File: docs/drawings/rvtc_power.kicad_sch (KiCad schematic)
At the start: 0 parts

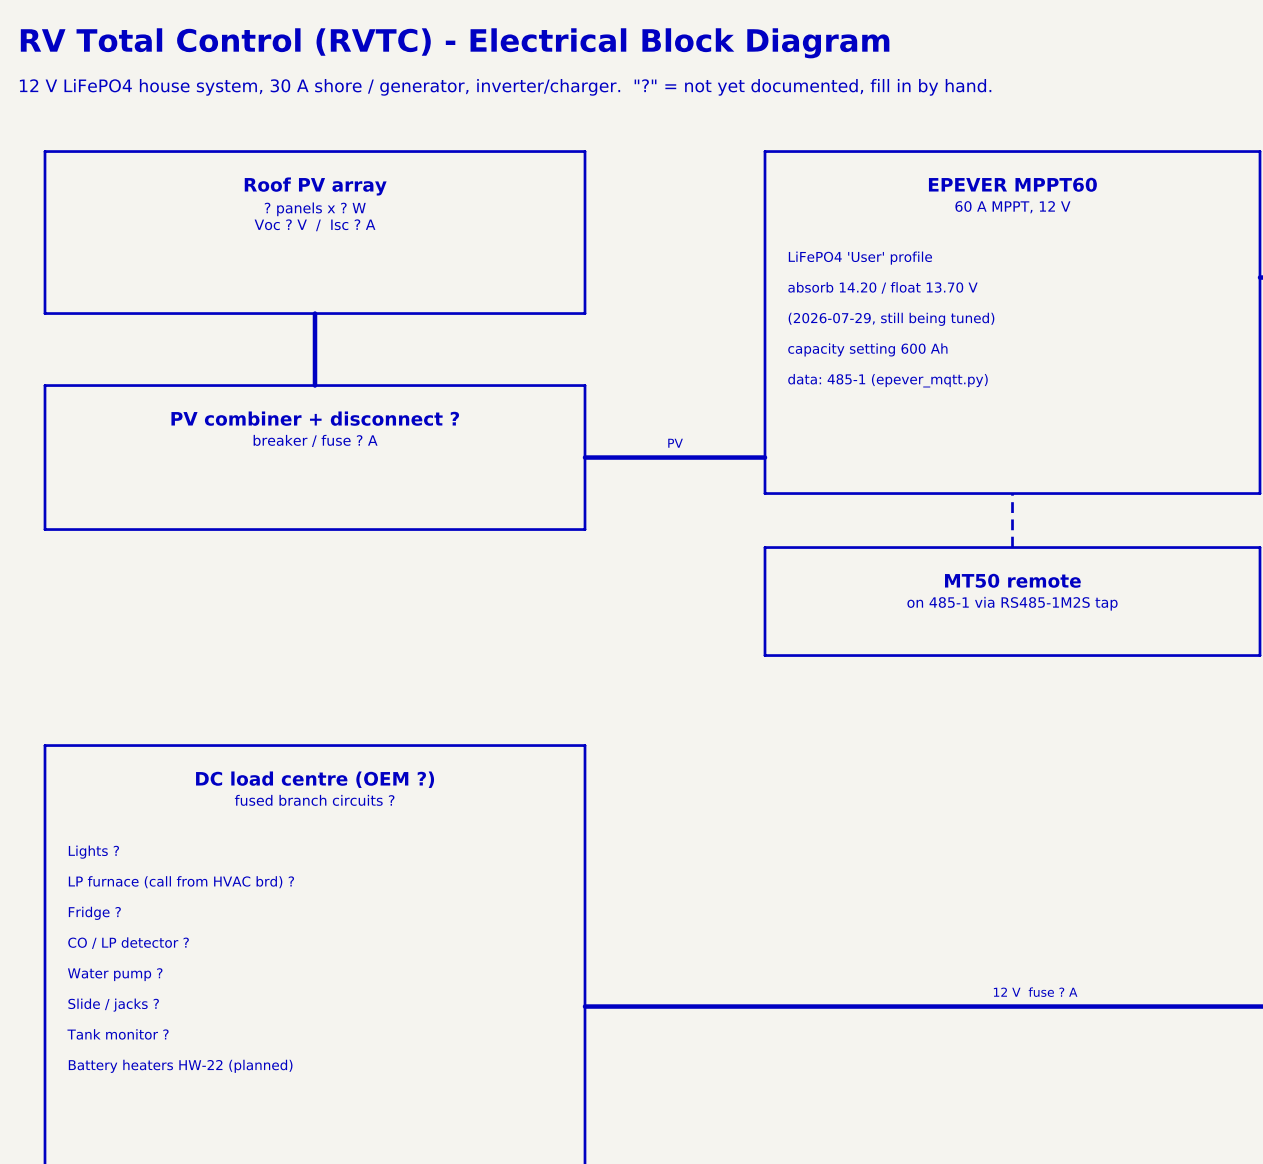
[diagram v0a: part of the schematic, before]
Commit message: Drawings: observer is a LilyGo T-Beam; fill in PV array from datasheet
Page 1: MeshCore Observer box now names VE7CBH-RVTC (LilyGo T-Beam,
DUQ, also reports to the public observer map) instead of "ESP32-S3".

Page 2 (includes the owner's hand edits so far, e.g. DC load centre
fuse 70 A and 3 string lines): PV array is 9 x Renogy RNG-100D-SS,
3S3P = 900 W; array Voc 72.9 V / Isc 15.6 A, Vmp 61.2 V / Imp 14.7 A
(from the panel datasheet). Combiner notes the 15 A panel max series
fuse rating.

Co-Authored-By: Claude Opus 5.5 <noreply@anthropic.com>
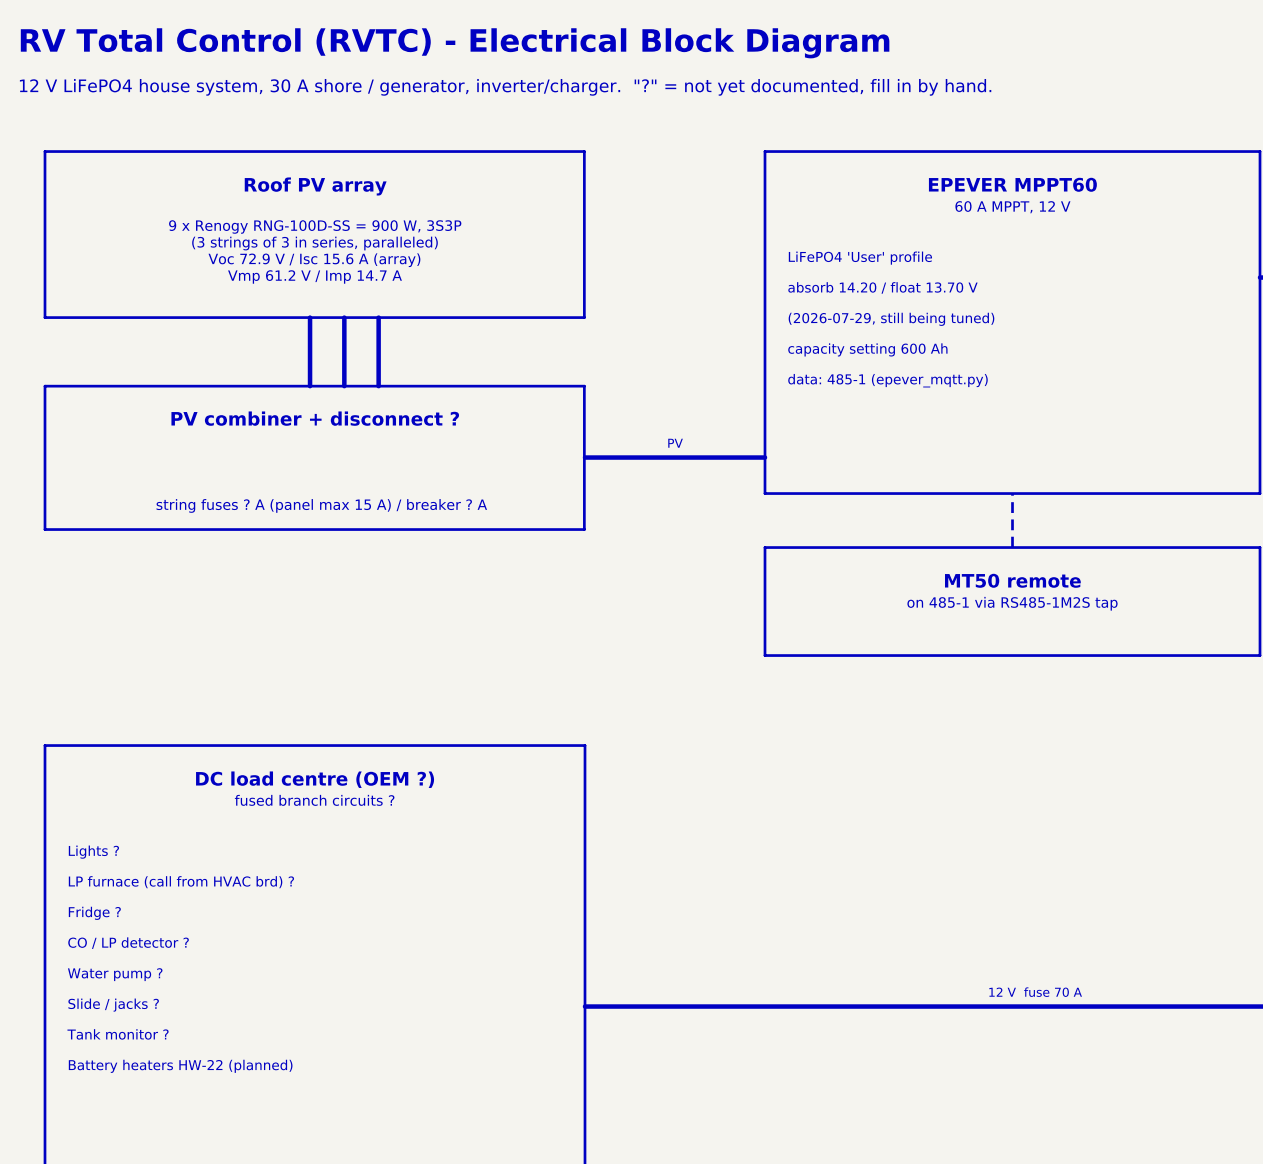
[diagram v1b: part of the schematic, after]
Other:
- note added: "12 V fuse 70 A"
- note added: "9 x Renogy RNG-100D-SS = 900 W, 3S3P (3 strings of 3 in series, paralleled) Voc 72.9 V / Isc 15.6 A (array) Vmp 61.2 V / Imp 14.7 A"
- note added: "string fuses ? A (panel max 15 A) / breaker ? A"
- note removed: "12 V fuse ? A"
- note removed: "? panels x ? W Voc ? V / Isc ? A"
- note removed: "breaker / fuse ? A"

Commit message: Drawings: 11x17, single Waveshare 8-port unit, two DC distributions
- Both sheets now USLedger (11x17); layouts compressed vertically to fit.
- Page 1: the eight 485-x gateways are one Waveshare 8-port RS-485/ETH
  unit (one IP per port), drawn as a single box like the HF5142B.
- Page 2: filled from the parts list (items carried over from the Cougar
  build): 350 A ANL main fuse + Ampper switch, ECO-WORTHY combiner (12 A
  per string), BlueFire fuse box, 30 A shore/gen cords + DIN breakers,
  WFCO OEM load centre, EVO-RC+ remote, Sony/Sceptre monitors. Flags the
  80 V-rated Americal DIN breaker vs ~86 V cold array Voc.
- Two DC distribution points: forward electrical bay bus bars and the
  WFCO OEM load centre, fed through a 250 A main DC fuse.
- Page 1 generator emits 11x17 directly.

Co-Authored-By: Claude Opus 5.5 <noreply@anthropic.com>
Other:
- note added: "2 x 30 A DIN brkr/disconnect + meter, DIN box auto transfer switch, or EVO AC-in priority ?"
- note added: "AC load centre (WFCO, OEM)"
- note added: "BlueFire 12-way blade fuse box, feed ? A - all 12 V"
- note added: "Bsomain ANL-350A + Ampper battery switch (S1)"
- note added: "ECO-WORTHY 4-string, 12 A brkr/string (3 used) Americal 50 A DC DIN brkr ? - rated 80 V!"
- note added: "Forward electrical bay - 12 V DC distribution - +/- bus bars ?"
- note added: "Generator inlet 30 A"
- note added: "Main fuse 350 A ANL"
- note added: "PV combiner + disconnect"
- note added: "Sony 32in HDMI TV/monitor Sceptre 16in (12 V PSU on AC) 1 via HDMI-over-Cat5e ? J45 speakers"
- note added: "Trailer DC distribution (WFCO, OEM)"
- note added: "Waveshare 8-port RS-485 gateway"
- note added: "inverter / charger, 12 V, EVO-RC+ remote"
- note added: "main DC fuse 250 A"
- note removed: "+ battery disconnect ?"
- note removed: "12 V DC distribution - +/- bus bars ?"
- note removed: "12 V fuse 70 A"
- note removed: "2 x J45 monitors (1 via HDMI-over-Cat5e) J45 speakers"
- note removed: "AC load centre (OEM ?)"
- note removed: "DC load centre (OEM ?)"
- note removed: "Generator inlet ? A"
- note removed: "Main fuse ? A"
- note removed: "PV combiner + disconnect ?"
- note removed: "Waveshare RS-485 gateways x8"
- note removed: "auto transfer switch, or EVO AC-in priority ?"
- note removed: "inverter / charger, 12 V"
- note removed: "own fused feed ? A - all RVTC kit is 12 V"
- note removed: "string fuses ? A (panel max 15 A) / breaker ? A"

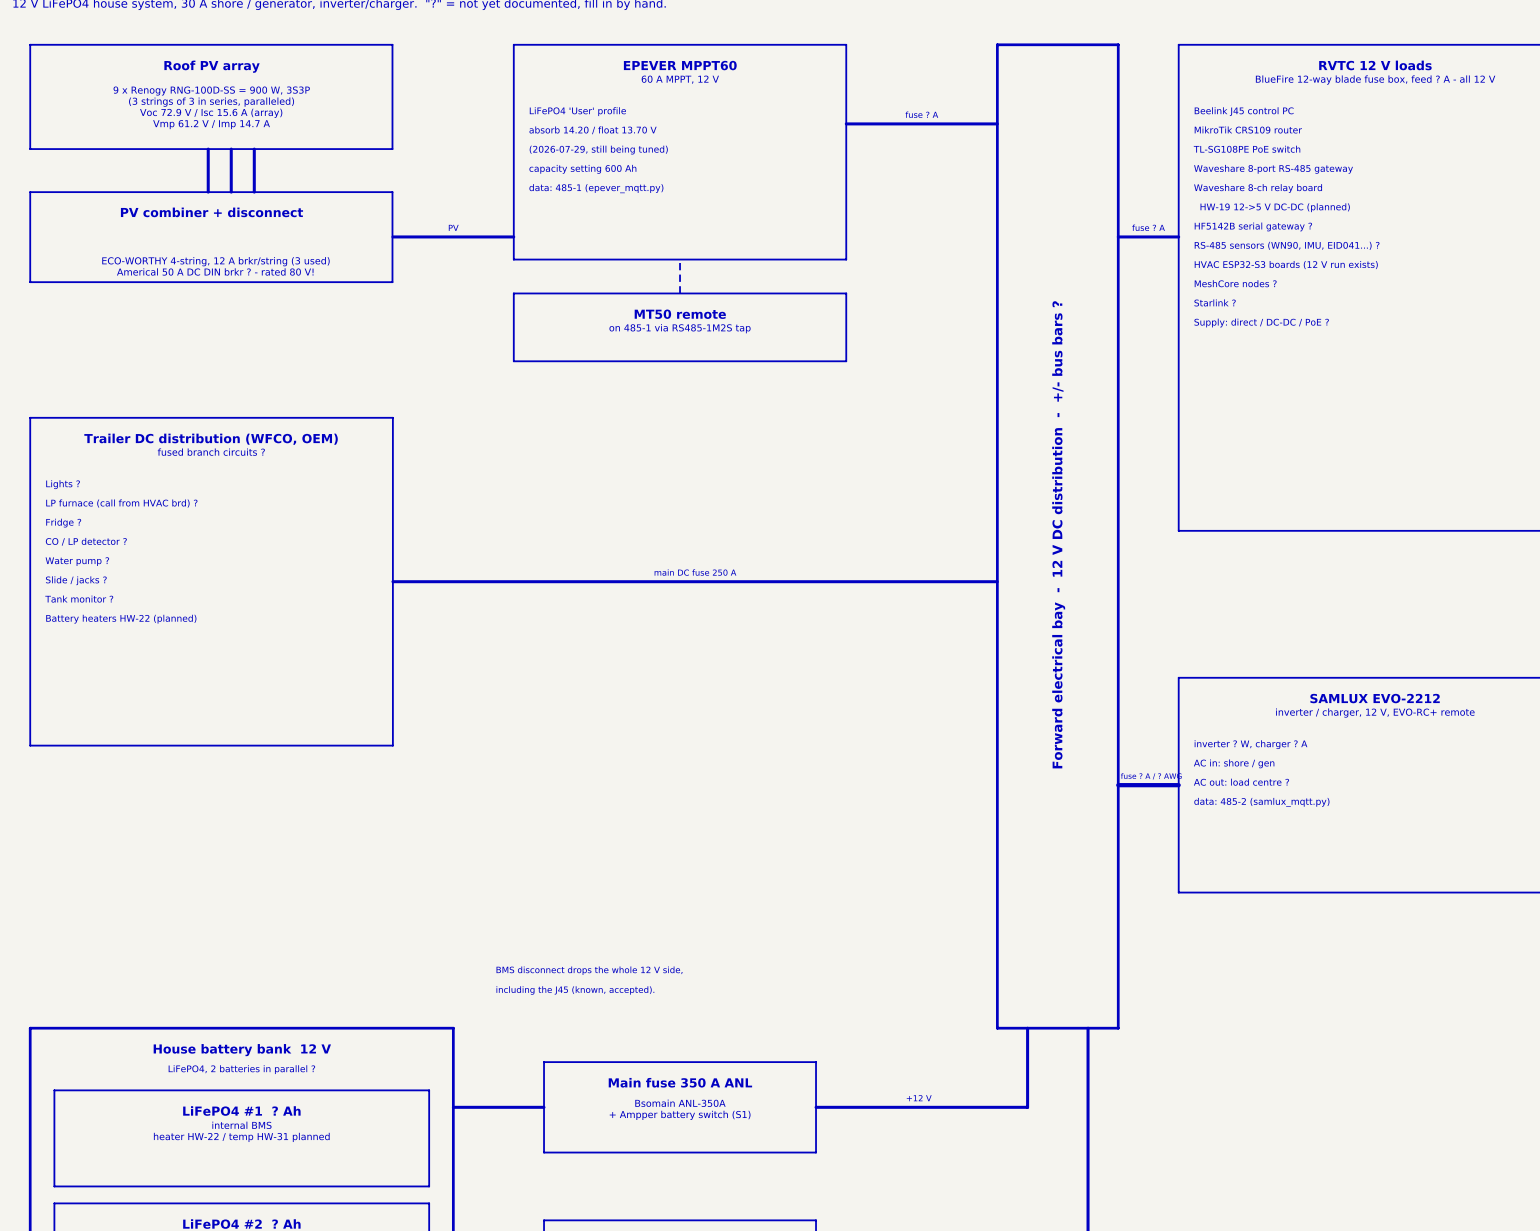
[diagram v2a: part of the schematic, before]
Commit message: Electrical sheet: correct breaker/fuse placement per owner
- PV combiner breakers rated 250 VDC (drops the 80 V warning).
- MPPT60 output: 50 A DC breaker (the Americal DIN unit).
- Ampper S1 + 350 A Class T feeds the EVO-2212 (battery isolation);
  Ampper S2 + 250 A ANL feeds the WFCO trailer DC distribution.
  No other ANL fuses in this build (old 70 A / 100 A were Cougar-only).
- Main battery fuse at the B+ terminal drawn as TBD (type and size).
- RVTC 12 V: 5 V 50 W PSU off the forward fuse block feeds a 5 V
  blade fuse block.

Co-Authored-By: Claude Opus 5.5 <noreply@anthropic.com>
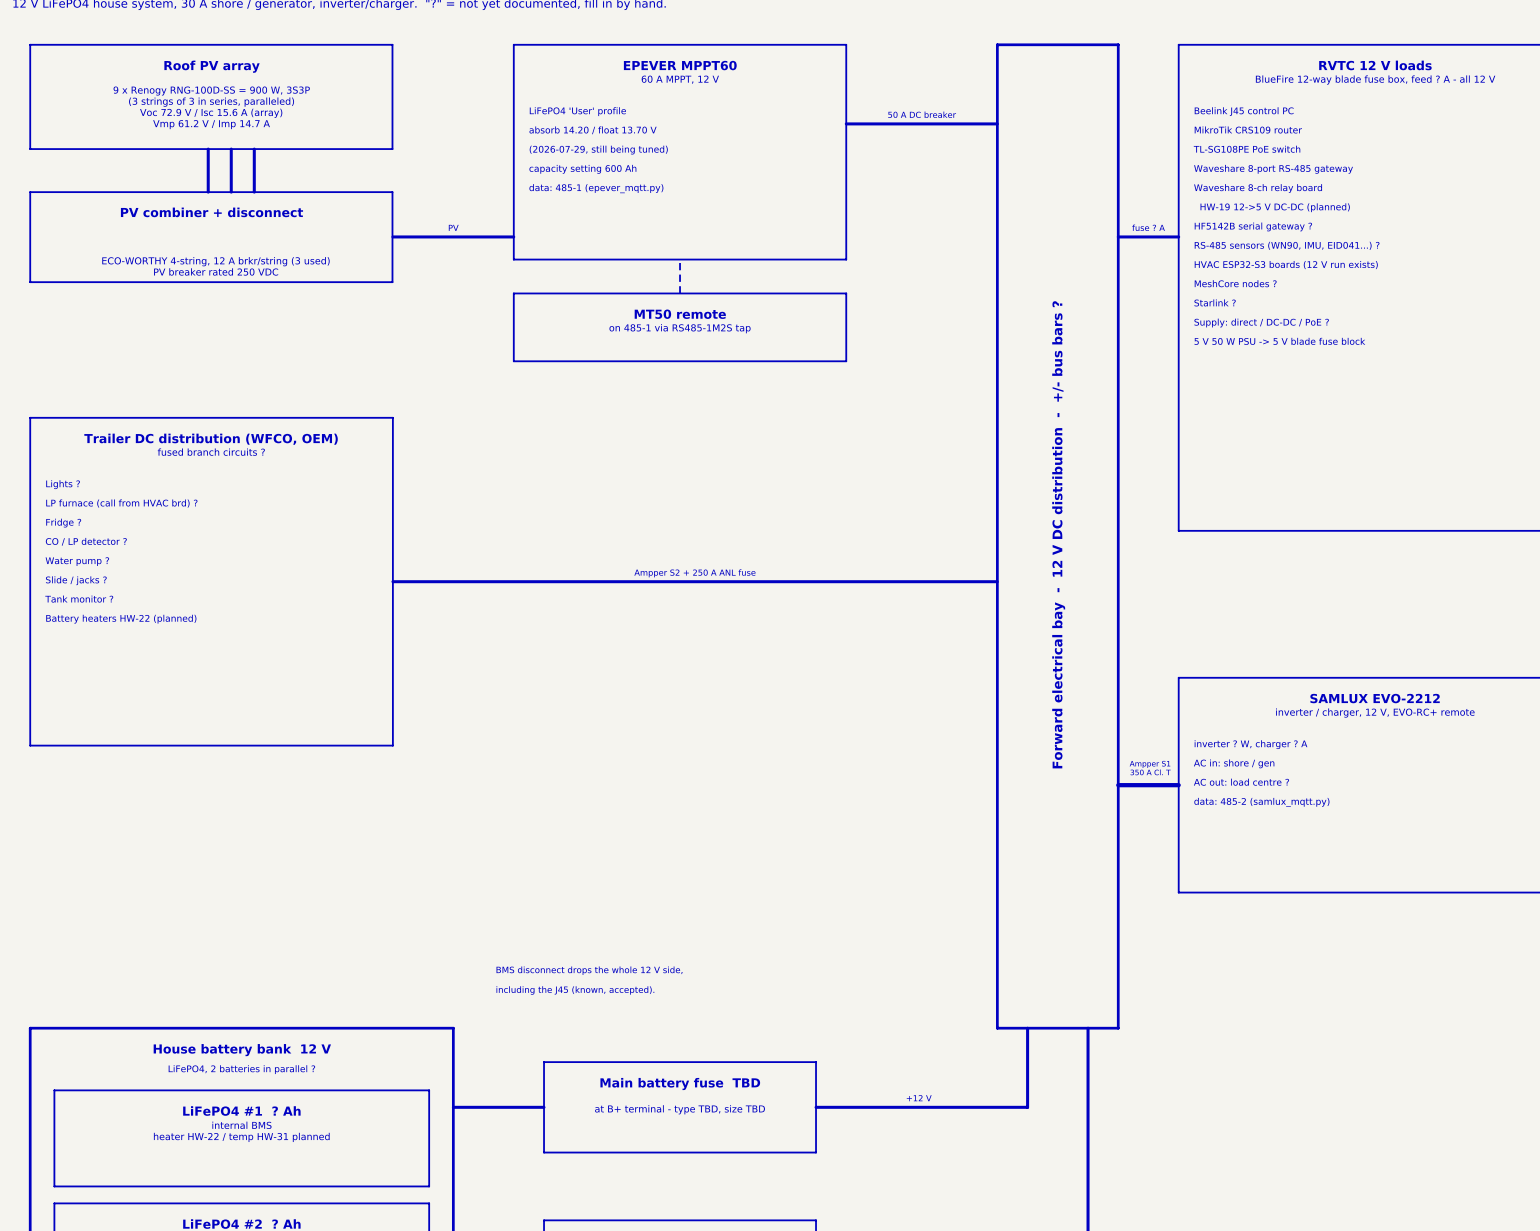
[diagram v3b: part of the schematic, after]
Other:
- note added: "5 V 50 W PSU -> 5 V blade fuse block"
- note added: "50 A DC breaker"
- note added: "Ampper S1 350 A Cl. T"
- note added: "Ampper S2 + 250 A ANL fuse"
- note added: "ECO-WORTHY 4-string, 12 A brkr/string (3 used) PV breaker rated 250 VDC"
- note added: "Main battery fuse TBD"
- note added: "at B+ terminal - type TBD, size TBD"
- note removed: "Bsomain ANL-350A + Ampper battery switch (S1)"
- note removed: "ECO-WORTHY 4-string, 12 A brkr/string (3 used) Americal 50 A DC DIN brkr ? - rated 80 V!"
- note removed: "Main fuse 350 A ANL"
- note removed: "fuse ? A / ? AWG"
- note removed: "main DC fuse 250 A"
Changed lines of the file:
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@@
+		)
+	)
+	(text "5 V 50 W PSU -> 5 V blade fuse block"
+		(exclude_from_sim no)
+		(at 207.5 74.33 0)
+		(effects
+			(font
+				(size 1.1 1.1)
+			)
+			(justify left)
 		)
 	)
@@
 		)
 	)
-	(text "fuse ? A / ? AWG"
-		(exclude_from_sim no)
-		(at 200.5 146.23 0)
+	(text "Ampper S1\n350 A Cl. T"
+		(exclude_from_sim no)
+		(at 200.3 144.9 0)
 		(effects
 			(font
@@
 		)
 	)
-	(text "ECO-WORTHY 4-string, 12 A brkr/string (3 used)\nAmerical 50 A DC DIN brkr ? - rated 80 V!"
+	(text "ECO-WORTHY 4-string, 12 A brkr/string (3 used)\nPV breaker rated 250 VDC"
 		(exclude_from_sim no)
 		(at 45.72 61.922 0)
@@
 		)
 	)
-	(text "Bsomain ANL-350A\n+ Ampper battery switch (S1)"
+	(text "at B+ terminal - type TBD, size TBD"
 		(exclude_from_sim no)
 		(at 122.5 201.301 0)
@@
 		)
 	)
-	(text "Main fuse 350 A ANL"
+	(text "Main battery fuse  TBD"
 		(exclude_from_sim no)
 		(at 122.5 197 0)
@@
 		)
 	)
-	(text "fuse ? A"
+	(text "50 A DC breaker"
 		(exclude_from_sim no)
 		(at 162.5 36.835 0)
@@
 		)
 	)
-	(text "main DC fuse 250 A"
+	(text "Ampper S2 + 250 A ANL fuse"
 		(exclude_from_sim no)
 		(at 125 112.57 0)
